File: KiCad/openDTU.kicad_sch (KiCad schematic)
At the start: 46 parts, among them J1 USB_C_Receptacle_USB2.0, J2 Conn_Coaxial, J3 Micro_SD_Card, J4 Conn_02x05_Counter_Clockwise, Q1 BC817, Q2 BC817, SW1 SW_Push, SW2 SW_Push, U1 CH340C, U3 ESP32-WROOM-32, U4 nRF24L01P, U5 NCP1117-3.3_SOT223, Y1 16 MHz

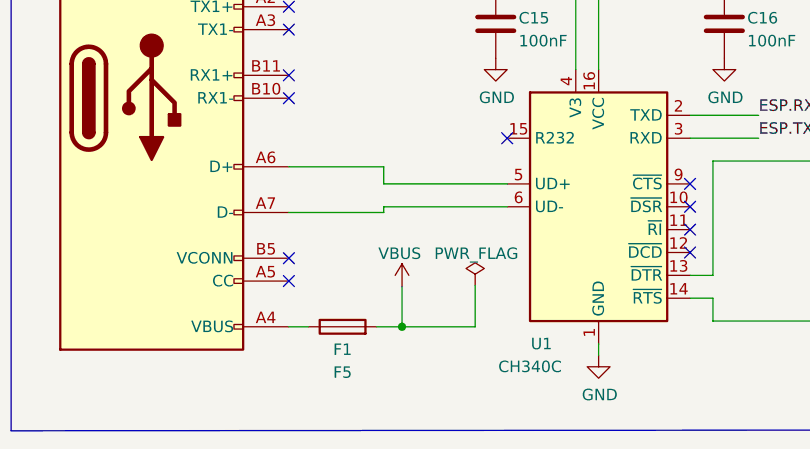
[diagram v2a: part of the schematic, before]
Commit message: adding 5k1 resistor for A5 and B5 of usb-c
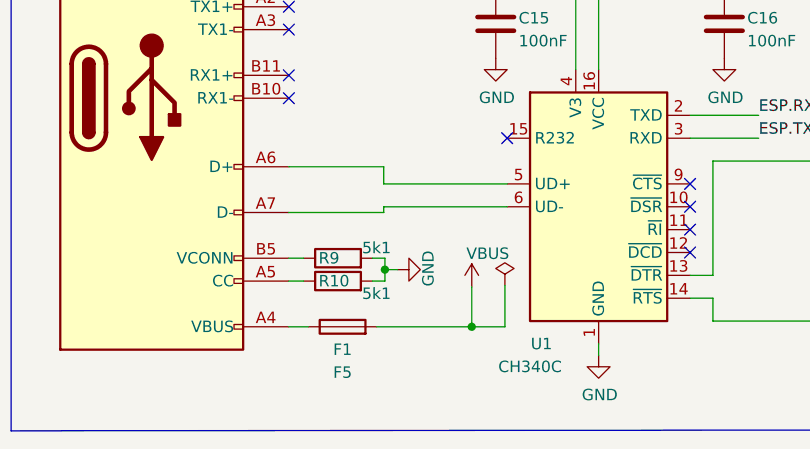
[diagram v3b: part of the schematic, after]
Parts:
- added R10, R9: 5k1, Resistor_SMD:R_0603_1608Metric, symbol Device:R
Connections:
- net GND: now also R10.2, R9.2
- net at J1.A5 (CC): now also R10.1
- net at J1.B5 (VCONN): now also R9.1
- no-connect marks 35 -> 33
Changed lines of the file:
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@@
   (junction (at 335.407 206.248) (diameter 0) (color 0 0 0 0)
   )
+  (junction (at 75.311 219.202) (diameter 0) (color 0 0 0 0)
+  )
   (junction (at 204.47 192.659) (diameter 0) (color 0 0 0 0)
   )
@@
   (junction (at 305.816 155.956) (diameter 0) (color 0 0 0 0)
   )
-  (junction (at 77.216 225.552) (diameter 0) (color 0 0 0 0)
+  (junction (at 84.963 225.552) (diameter 0) (color 0 0 0 0)
   )
   (junction (at 317.881 193.929) (diameter 0) (color 0 0 0 0)
@@
   (no_connect (at 64.643 167.132))
   (no_connect (at 64.643 169.672))
-  (no_connect (at 64.643 217.932))
-  (no_connect (at 64.643 220.472))
   (no_connect (at 88.9 204.597))
   (no_connect (at 89.535 95.25))
@@
     (stroke (width 0) (type default) (color 0 0 0 0))
   )
-  (wire (pts (xy 85.344 220.98) (xy 85.344 225.552))
+  (wire (pts (xy 88.646 220.98) (xy 88.646 225.552))
     (stroke (width 0) (type default) (color 0 0 0 0))
   )
@@
     (stroke (width 0) (type default) (color 0 0 0 0))
   )
+  (wire (pts (xy 64.643 220.472) (xy 66.294 220.472))
+    (stroke (width 0) (type default) (color 0 0 0 0))
+  )
   (wire (pts (xy 185.547 108.839) (xy 185.547 110.109))
     (stroke (width 0) (type default) (color 0 0 0 0))
@@
     (stroke (width 0) (type default) (color 0 0 0 0))
   )
-  (wire (pts (xy 77.216 225.552) (xy 85.344 225.552))
+  (wire (pts (xy 84.963 225.552) (xy 88.646 225.552))
     (stroke (width 0) (type default) (color 0 0 0 0))
   )
@@
     (stroke (width 0) (type default) (color 0 0 0 0))
   )
+  (wire (pts (xy 75.311 219.202) (xy 76.708 219.202))
+    (stroke (width 0) (type default) (color 0 0 0 0))
+  )
   (wire (pts (xy 374.2436 202.946) (xy 386.7404 202.946))
     (stroke (width 0) (type default) (color 0 0 0 0))
@@
     (stroke (width 0) (type default) (color 0 0 0 0))
   )
+  (wire (pts (xy 73.914 220.472) (xy 75.311 220.472))
+    (stroke (width 0) (type default) (color 0 0 0 0))
+  )
   (wire (pts (xy 379.9332 197.866) (xy 374.2436 197.866))
     (stroke (width 0) (type default) (color 0 0 0 0))
@@
     (stroke (width 0) (type default) (color 0 0 0 0))
   )
+  (wire (pts (xy 75.311 220.472) (xy 75.311 219.202))
+    (stroke (width 0) (type default) (color 0 0 0 0))
+  )
   (polyline (pts (xy 185.039 236.982) (xy 282.829 236.982))
     (stroke (width 0) (type default) (color 0 0 0 0))
@@
     (stroke (width 0) (type default) (color 0 0 0 0))
   )
-  (wire (pts (xy 74.422 225.552) (xy 77.216 225.552))
+  (wire (pts (xy 74.422 225.552) (xy 84.963 225.552))
     (stroke (width 0) (type default) (color 0 0 0 0))
   )
@@
     (stroke (width 0) (type default) (color 0 0 0 0))
   )
-  (wire (pts (xy 77.216 225.552) (xy 77.216 221.107))
+  (wire (pts (xy 84.963 225.552) (xy 84.963 221.107))
     (stroke (width 0) (type default) (color 0 0 0 0))
   )
@@
     (stroke (width 0) (type default) (color 0 0 0 0))
   )
+  (wire (pts (xy 64.643 217.932) (xy 66.294 217.932))
+    (stroke (width 0) (type default) (color 0 0 0 0))
+  )
   (bus (pts (xy 348.742 155.956) (xy 348.742 197.866))
     (stroke (width 0) (type default) (color 0 0 0 0))
@@
   )
   (wire (pts (xy 89.535 69.85) (xy 103.378 69.85))
+    (stroke (width 0) (type default) (color 0 0 0 0))
+  )
+  (wire (pts (xy 75.311 217.932) (xy 75.311 219.202))
+    (stroke (width 0) (type default) (color 0 0 0 0))
+  )
+  (wire (pts (xy 73.914 217.932) (xy 75.311 217.932))
     (stroke (width 0) (type default) (color 0 0 0 0))
   )
@@
     (pin "2")
   )
-  (symbol (lib_id "power:VBUS") (at 77.216 221.107 0) (unit 1)
-    (in_bom yes) (on_board yes)
-    (property "Reference" "#PWR021" (id 0) (at 77.216 224.917 0)
-      (effects (font (size 1.27 1.27)) hide)
-    )
-    (property "Value" "VBUS" (id 1) (at 76.962 217.424 0))
-    (property "Footprint" "" (id 2) (at 77.216 221.107 0)
-      (effects (font (size 1.27 1.27)) hide)
-    )
-    (property "Datasheet" "" (id 3) (at 77.216 221.107 0)
+  (symbol (lib_id "power:VBUS") (at 84.963 221.107 0) (unit 1)
+    (in_bom yes) (on_board yes)
+    (property "Reference" "#PWR021" (id 0) (at 84.963 224.917 0)
+      (effects (font (size 1.27 1.27)) hide)
+    )
+    (property "Value" "VBUS" (id 1) (at 86.741 217.424 0))
+    (property "Footprint" "" (id 2) (at 84.963 221.107 0)
+      (effects (font (size 1.27 1.27)) hide)
+    )
+    (property "Datasheet" "" (id 3) (at 84.963 221.107 0)
       (effects (font (size 1.27 1.27)) hide)
     )
@@
     (pin "1")
   )
+  (symbol (lib_id "power:GND") (at 76.708 219.202 90) (unit 1)
+    (in_bom yes) (on_board yes)
+    (property "Reference" "#PWR027" (id 0) (at 83.058 219.202 0)
+      (effects (font (size 1.27 1.27)) hide)
+    )
+    (property "Value" "GND" (id 1) (at 80.137 219.075 0))
+    (property "Footprint" "" (id 2) (at 76.708 219.202 0)
+      (effects (font (size 1.27 1.27)) hide)
+    )
+    (property "Datasheet" "" (id 3) (at 76.708 219.202 0)
+      (effects (font (size 1.27 1.27)) hide)
+    )
+    (pin "1")
+  )
   (symbol (lib_id "Transistor_BJT:BC817") (at 147.32 224.917 0) (mirror x) (unit 1)
     (in_bom yes) (on_board yes)
@@
     )
     (pin "1")
+  )
+  (symbol (lib_id "Device:R") (at 70.104 217.932 90) (unit 1)
+    (in_bom yes) (on_board yes)
+    (property "Reference" "R9" (id 0) (at 67.945 217.932 90)
+      (effects (font (size 1.27 1.27)) (justify right))
+    )
+    (property "Value" "5k1" (id 1) (at 72.771 216.789 90)
+      (effects (font (size 1.27 1.27)) (justify right))
+    )
+    (property "Footprint" "Resistor_SMD:R_0603_1608Metric" (id 2) (at 70.104 219.71 90)
+      (effects (font (size 1.27 1.27)) hide)
+    )
+    (property "Datasheet" "~" (id 3) (at 70.104 217.932 0)
+      (effects (font (size 1.27 1.27)) hide)
+    )
+    (pin "1")
+    (pin "2")
   )
   (symbol (lib_id "Transistor_BJT:BC817") (at 147.32 207.137 0) (unit 1)
@@
     (pin "2")
   )
+  (symbol (lib_id "Device:R") (at 70.104 220.472 90) (unit 1)
+    (in_bom yes) (on_board yes)
+    (property "Reference" "R10" (id 0) (at 67.945 220.472 90)
+      (effects (font (size 1.27 1.27)) (justify right))
+    )
+    (property "Value" "5k1" (id 1) (at 72.771 221.869 90)
+      (effects (font (size 1.27 1.27)) (justify right))
+    )
+    (property "Footprint" "Resistor_SMD:R_0603_1608Metric" (id 2) (at 70.104 222.25 90)
+      (effects (font (size 1.27 1.27)) hide)
+    )
+    (property "Datasheet" "~" (id 3) (at 70.104 220.472 0)
+      (effects (font (size 1.27 1.27)) hide)
+    )
+    (pin "1")
+    (pin "2")
+  )
   (symbol (lib_id "Device:R") (at 317.881 181.483 0) (unit 1)
     (in_bom yes) (on_board yes) (fields_autoplaced)
@@
     (pin "1")
   )
-  (symbol (lib_id "power:PWR_FLAG") (at 85.344 220.98 0) (unit 1)
-    (in_bom yes) (on_board yes)
-    (property "Reference" "#FLG0102" (id 0) (at 85.344 219.075 0)
-      (effects (font (size 1.27 1.27)) hide)
-    )
-    (property "Value" "PWR_FLAG" (id 1) (at 85.471 217.424 0))
-    (property "Footprint" "" (id 2) (at 85.344 220.98 0)
-      (effects (font (size 1.27 1.27)) hide)
-    )
-    (property "Datasheet" "~" (id 3) (at 85.344 220.98 0)
+  (symbol (lib_id "power:PWR_FLAG") (at 88.646 220.98 0) (unit 1)
+    (in_bom yes) (on_board yes)
+    (property "Reference" "#FLG0102" (id 0) (at 88.646 219.075 0)
+      (effects (font (size 1.27 1.27)) hide)
+    )
+    (property "Value" "PWR_FLAG" (id 1) (at 88.773 217.424 0)
+      (effects (font (size 1.27 1.27)) hide)
+    )
+    (property "Footprint" "" (id 2) (at 88.646 220.98 0)
+      (effects (font (size 1.27 1.27)) hide)
+    )
+    (property "Datasheet" "~" (id 3) (at 88.646 220.98 0)
       (effects (font (size 1.27 1.27)) hide)
     )
@@
       (reference "#PWR026") (unit 1) (value "GND") (footprint "")
     )
+    (path "/741bd836-1398-46a2-909c-20e5bde4ede8"
+      (reference "#PWR027") (unit 1) (value "GND") (footprint "")
+    )
     (path "/146e1e78-9ed5-4a55-ad5c-4176d7e1be8b"
       (reference "#PWR0101") (unit 1) (value "GND") (footprint "")
@@
       (reference "R8") (unit 1) (value "10k") (footprint "Resistor_SMD:R_0603_1608Metric")
     )
+    (path "/8e233198-1ea8-4a3a-98c0-8d599041add5"
+      (reference "R9") (unit 1) (value "5k1") (footprint "Resistor_SMD:R_0603_1608Metric")
+    )
+    (path "/c6bae959-6189-4396-a451-aa44fd762884"
+      (reference "R10") (unit 1) (value "5k1") (footprint "Resistor_SMD:R_0603_1608Metric")
+    )
     (path "/6ff503e4-9445-4c27-ae98-ef813007051a"

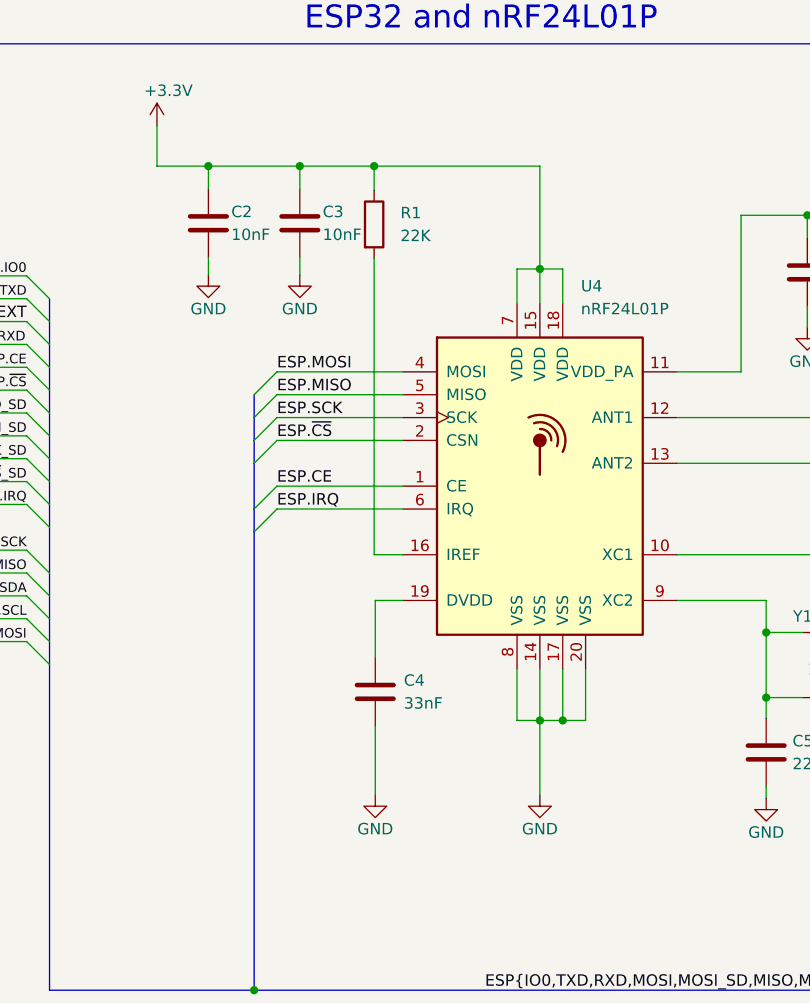
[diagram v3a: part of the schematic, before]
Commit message: first batch of smt variant ordered
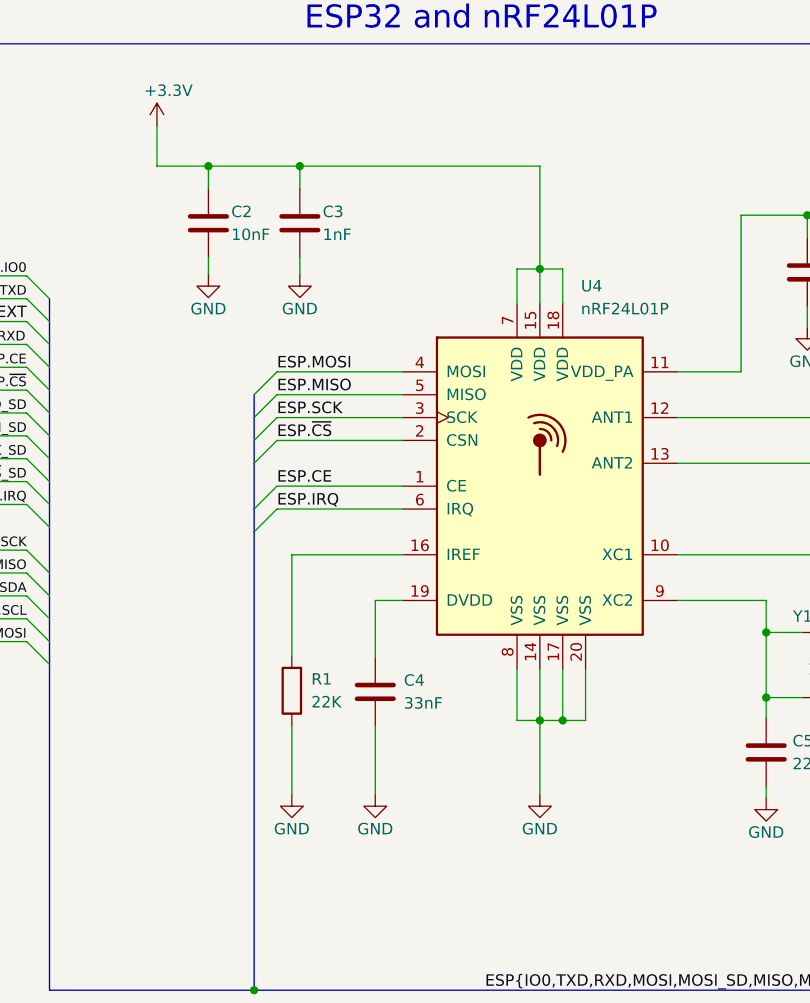
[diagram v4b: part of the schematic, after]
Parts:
- C3: value 10nF -> 1nF
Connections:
- net +3.3V: no longer R1.1
- net GND: now also R1.1
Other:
- moved on the sheet: R1
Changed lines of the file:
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@@
   (junction (at 74.295 121.285) (diameter 0) (color 0 0 0 0)
-  )
-  (junction (at 141.986 39.878) (diameter 0) (color 0 0 0 0)
   )
   (junction (at 358.7496 189.611) (diameter 0) (color 0 0 0 0)
@@
     (stroke (width 0) (type default) (color 0 0 0 0))
   )
-  (wire (pts (xy 133.731 39.878) (xy 141.986 39.878))
+  (wire (pts (xy 133.731 39.878) (xy 160.401 39.878))
     (stroke (width 0) (type default) (color 0 0 0 0))
   )
@@
     (stroke (width 0) (type default) (color 0 0 0 0))
   )
+  (wire (pts (xy 132.842 101.981) (xy 132.842 109.728))
+    (stroke (width 0) (type default) (color 0 0 0 0))
+  )
   (wire (pts (xy 44.958 156.845) (xy 49.403 156.845))
     (stroke (width 0) (type default) (color 0 0 0 0))
@@
     (stroke (width 0) (type default) (color 0 0 0 0))
   )
-  (wire (pts (xy 141.986 50.165) (xy 141.986 83.058))
+  (wire (pts (xy 132.842 94.361) (xy 132.842 83.058))
     (stroke (width 0) (type default) (color 0 0 0 0))
   )
@@
     (stroke (width 0) (type default) (color 0 0 0 0))
   )
-  (wire (pts (xy 141.986 83.058) (xy 145.161 83.058))
-    (stroke (width 0) (type default) (color 0 0 0 0))
-  )
   (bus (pts (xy 305.816 183.007) (xy 305.816 187.833))
     (stroke (width 0) (type default) (color 0 0 0 0))
@@
     (stroke (width 0) (type default) (color 0 0 0 0))
   )
+  (wire (pts (xy 132.842 83.058) (xy 145.161 83.058))
+    (stroke (width 0) (type default) (color 0 0 0 0))
+  )
   (polyline (pts (xy 282.829 26.289) (xy 282.829 136.779))
     (stroke (width 0) (type default) (color 0 0 0 0))
@@
     (stroke (width 0) (type default) (color 0 0 0 0))
   )
-  (wire (pts (xy 141.986 39.878) (xy 160.401 39.878))
-    (stroke (width 0) (type default) (color 0 0 0 0))
-  )
   (polyline (pts (xy 393.7 136.8552) (xy 285.877 136.779))
     (stroke (width 0) (type default) (color 0 0 0 0))
@@
   )
   (wire (pts (xy 329.946 194.945) (xy 329.946 193.929))
-    (stroke (width 0) (type default) (color 0 0 0 0))
-  )
-  (wire (pts (xy 141.986 39.878) (xy 141.986 42.545))
     (stroke (width 0) (type default) (color 0 0 0 0))
   )
@@
       (effects (font (size 1.27 1.27)) (justify left))
     )
-    (property "Value" "10nF" (id 1) (at 136.271 47.498 0)
+    (property "Value" "1nF" (id 1) (at 136.271 47.498 0)
       (effects (font (size 1.27 1.27)) (justify left))
     )
@@
     (pin "1")
     (pin "2")
+  )
+  (symbol (lib_id "power:GND") (at 132.842 109.728 0) (unit 1)
+    (in_bom yes) (on_board yes)
+    (property "Reference" "#PWR0115" (id 0) (at 132.842 116.078 0)
+      (effects (font (size 1.27 1.27)) hide)
+    )
+    (property "Value" "GND" (id 1) (at 132.842 113.538 0))
+    (property "Footprint" "" (id 2) (at 132.842 109.728 0)
+      (effects (font (size 1.27 1.27)) hide)
+    )
+    (property "Datasheet" "" (id 3) (at 132.842 109.728 0)
+      (effects (font (size 1.27 1.27)) hide)
+    )
+    (pin "1")
   )
   (symbol (lib_id "Device:R") (at 317.881 181.483 0) (unit 1)
@@
     (pin "9")
   )
-  (symbol (lib_id "Device:R") (at 141.986 46.355 0) (unit 1)
+  (symbol (lib_id "Device:R") (at 132.842 98.171 180) (unit 1)
     (in_bom yes) (on_board yes) (fields_autoplaced)
-    (property "Reference" "R1" (id 0) (at 144.907 45.0849 0)
-      (effects (font (size 1.27 1.27)) (justify left))
-    )
-    (property "Value" "22K" (id 1) (at 144.907 47.6249 0)
-      (effects (font (size 1.27 1.27)) (justify left))
-    )
-    (property "Footprint" "Resistor_SMD:R_0603_1608Metric_Pad0.98x0.95mm_HandSolder" (id 2) (at 140.208 46.355 90)
-      (effects (font (size 1.27 1.27)) hide)
-    )
-    (property "Datasheet" "~" (id 3) (at 141.986 46.355 0)
+    (property "Reference" "R1" (id 0) (at 135.001 96.9009 0)
+      (effects (font (size 1.27 1.27)) (justify right))
+    )
+    (property "Value" "22K" (id 1) (at 135.001 99.4409 0)
+      (effects (font (size 1.27 1.27)) (justify right))
+    )
+    (property "Footprint" "Resistor_SMD:R_0603_1608Metric_Pad0.98x0.95mm_HandSolder" (id 2) (at 134.62 98.171 90)
+      (effects (font (size 1.27 1.27)) hide)
+    )
+    (property "Datasheet" "~" (id 3) (at 132.842 98.171 0)
       (effects (font (size 1.27 1.27)) hide)
     )
@@
       (reference "#PWR0114") (unit 1) (value "+3.3V") (footprint "")
     )
+    (path "/c792cd72-1b10-4013-ac32-cd398e138778"
+      (reference "#PWR0115") (unit 1) (value "GND") (footprint "")
+    )
     (path "/883cada5-36b1-4829-bf6c-a23fe5e54384"
       (reference "C1") (unit 1) (value "100nF") (footprint "Capacitor_SMD:C_0603_1608Metric_Pad1.08x0.95mm_HandSolder")
@@
     )
     (path "/c5847144-b410-496e-9efc-573ee2dd0a76"
-      (reference "C3") (unit 1) (value "10nF") (footprint "Capacitor_SMD:C_0603_1608Metric_Pad1.08x0.95mm_HandSolder")
+      (reference "C3") (unit 1) (value "1nF") (footprint "Capacitor_SMD:C_0603_1608Metric_Pad1.08x0.95mm_HandSolder")
     )
     (path "/38b8cbb0-de49-45a0-8678-c55a5ebc9eb4"
